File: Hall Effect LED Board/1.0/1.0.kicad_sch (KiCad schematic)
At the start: 5 parts, among them J1 Conn_01x04_Pin, U1 US5881LSE-AAA-000-RE

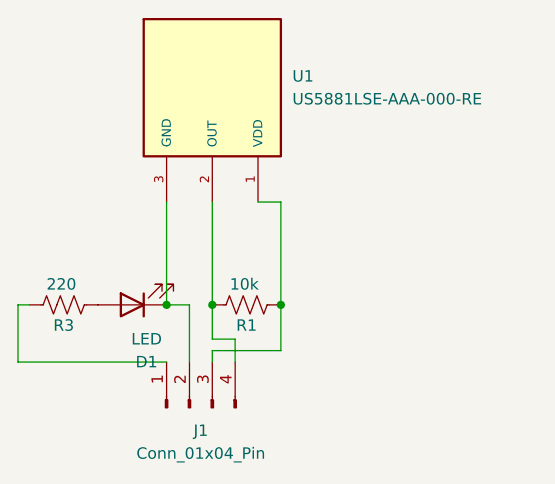
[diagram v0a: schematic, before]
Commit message: Set relative project specific components
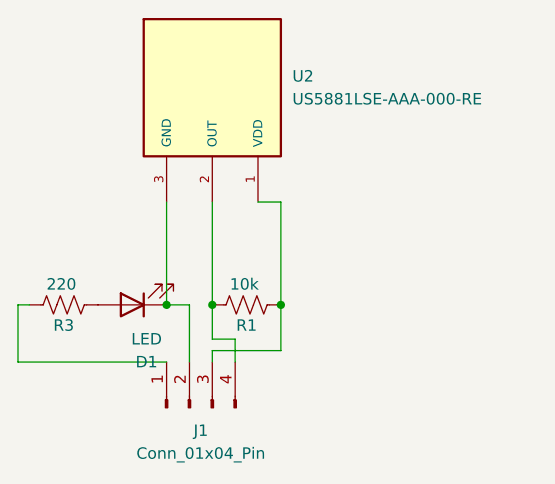
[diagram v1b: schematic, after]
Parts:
- removed U1: US5881LSE-AAA-000-RE, US5881LSE-AAA-000-RE:SOT95P280X100-3N, symbol US5881LSE-AAA-000-RE:US5881LSE-AAA-000-RE
- added U2: US5881LSE-AAA-000-RE, US5881LSE-AAA-000-RE:SOT95P280X100-3N, symbol US5881LSE-AAA-000-RE:US5881LSE-AAA-000-RE
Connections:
- net at J1.3 (Pin_3), R1.2: now also U2.1 (VDD)
- net at J1.4 (Pin_4), R1.1: now also U2.2 (OUT)
- net at D1.1 (K), J1.2 (Pin_2): now also U2.3 (GND)
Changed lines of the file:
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@@
-	)
-	(symbol
-		(lib_id "US5881LSE-AAA-000-RE:US5881LSE-AAA-000-RE")
-		(at 107.95 91.44 270)
-		(unit 1)
-		(exclude_from_sim no)
-		(in_bom yes)
-		(on_board yes)
-		(dnp no)
-		(fields_autoplaced yes)
-		(property "Reference" "U1"
-			(at 116.84 90.1699 90)
-			(effects
-				(font
-					(size 1.27 1.27)
-				)
-				(justify left)
-			)
-		)
-		(property "Value" "US5881LSE-AAA-000-RE"
-			(at 116.84 92.7099 90)
-			(effects
-				(font
-					(size 1.27 1.27)
-				)
-				(justify left)
-			)
-		)
-		(property "Footprint" "US5881LSE-AAA-000-RE:SOT95P280X100-3N"
-			(at 107.95 91.44 0)
-			(effects
-				(font
-					(size 1.27 1.27)
-				)
-				(justify bottom)
-				(hide yes)
-			)
-		)
-		(property "Datasheet" ""
-			(at 107.95 91.44 0)
-			(effects
-				(font
-					(size 1.27 1.27)
-				)
-				(hide yes)
-			)
-		)
-		(property "Description" ""
-			(at 107.95 91.44 0)
-			(effects
-				(font
-					(size 1.27 1.27)
-				)
-				(hide yes)
-			)
-		)
-		(property "MF" "Melexis"
-			(at 107.95 91.44 0)
-			(effects
-				(font
-					(size 1.27 1.27)
-				)
-				(justify bottom)
-				(hide yes)
-			)
-		)
-		(property "MAXIMUM_PACKAGE_HEIGHT" "1.00mm"
-			(at 107.95 91.44 0)
-			(effects
-				(font
-					(size 1.27 1.27)
-				)
-				(justify bottom)
-				(hide yes)
-			)
-		)
-		(property "Package" "TSOT-23L-3 Melexis"
-			(at 107.95 91.44 0)
-			(effects
-				(font
-					(size 1.27 1.27)
-				)
-				(justify bottom)
-				(hide yes)
-			)
-		)
-		(property "Price" "None"
-			(at 107.95 91.44 0)
-			(effects
-				(font
-					(size 1.27 1.27)
-				)
-				(justify bottom)
-				(hide yes)
-			)
-		)
-		(property "Check_prices" "https://www.snapeda.com/parts/US5881LSE-AAA-000-RE/Melexis/view-part/?ref=eda"
-			(at 107.95 91.44 0)
-			(effects
-				(font
-					(size 1.27 1.27)
-				)
-				(justify bottom)
-				(hide yes)
-			)
-		)
-		(property "STANDARD" "IPC-7351B"
-			(at 107.95 91.44 0)
-			(effects
-				(font
-					(size 1.27 1.27)
-				)
-				(justify bottom)
-				(hide yes)
-			)
-		)
-		(property "PARTREV" "005"
-			(at 107.95 91.44 0)
-			(effects
-				(font
-					(size 1.27 1.27)
-				)
-				(justify bottom)
-				(hide yes)
-			)
-		)
-		(property "SnapEDA_Link" "https://www.snapeda.com/parts/US5881LSE-AAA-000-RE/Melexis/view-part/?ref=snap"
-			(at 107.95 91.44 0)
-			(effects
-				(font
-					(size 1.27 1.27)
-				)
-				(justify bottom)
-				(hide yes)
-			)
-		)
-		(property "MP" "US5881LSE-AAA-000-RE"
-			(at 107.95 91.44 0)
-			(effects
-				(font
-					(size 1.27 1.27)
-				)
-				(justify bottom)
-				(hide yes)
-			)
-		)
-		(property "Description_1" "3 wire Latch"
-			(at 107.95 91.44 0)
-			(effects
-				(font
-					(size 1.27 1.27)
-				)
-				(justify bottom)
-				(hide yes)
-			)
-		)
-		(property "Availability" "In Stock"
-			(at 107.95 91.44 0)
-			(effects
-				(font
-					(size 1.27 1.27)
-				)
-				(justify bottom)
-				(hide yes)
-			)
-		)
-		(property "MANUFACTURER" "Melexis"
-			(at 107.95 91.44 0)
-			(effects
-				(font
-					(size 1.27 1.27)
-				)
-				(justify bottom)
-				(hide yes)
-			)
-		)
-		(pin "1"
-		)
-		(pin "3"
-		)
-		(pin "2"
-		)
-		(instances
-			(project ""
-				(path "/65e50814-7ec2-4aed-9027-cf46a8554e87"
-					(reference "U1")
-					(unit 1)
-				)
-			)
-		)
 	)
 	(symbol
@@
 					(unit 1)
 				)
+			)
+		)
+	)
+	(symbol
+		(lib_id "US5881LSE-AAA-000-RE:US5881LSE-AAA-000-RE")
+		(at 107.95 91.44 270)
+		(unit 1)
+		(exclude_from_sim no)
+		(in_bom yes)
+		(on_board yes)
+		(dnp no)
+		(fields_autoplaced yes)
+		(property "Reference" "U2"
+			(at 116.84 90.1699 90)
+			(effects
+				(font
+					(size 1.27 1.27)
+				)
+				(justify left)
+			)
+		)
+		(property "Value" "US5881LSE-AAA-000-RE"
+			(at 116.84 92.7099 90)
+			(effects
+				(font
+					(size 1.27 1.27)
+				)
+				(justify left)
+			)
+		)
+		(property "Footprint" "US5881LSE-AAA-000-RE:SOT95P280X100-3N"
+			(at 107.95 91.44 0)
+			(effects
+				(font
+					(size 1.27 1.27)
+				)
+				(justify bottom)
+				(hide yes)
+			)
+		)
+		(property "Datasheet" ""
+			(at 107.95 91.44 0)
+			(effects
+				(font
+					(size 1.27 1.27)
+				)
+				(hide yes)
+			)
+		)
+		(property "Description" ""
+			(at 107.95 91.44 0)
+			(effects
+				(font
+					(size 1.27 1.27)
+				)
+				(hide yes)
+			)
+		)
+		(property "MF" "Melexis"
+			(at 107.95 91.44 0)
+			(effects
+				(font
+					(size 1.27 1.27)
+				)
+				(justify bottom)
+				(hide yes)
+			)
+		)
+		(property "MAXIMUM_PACKAGE_HEIGHT" "1.00mm"
+			(at 107.95 91.44 0)
+			(effects
+				(font
+					(size 1.27 1.27)
+				)
+				(justify bottom)
+				(hide yes)
+			)
+		)
+		(property "Package" "TSOT-23L-3 Melexis"
+			(at 107.95 91.44 0)
+			(effects
+				(font
+					(size 1.27 1.27)
+				)
+				(justify bottom)
+				(hide yes)
+			)
+		)
+		(property "Price" "None"
+			(at 107.95 91.44 0)
+			(effects
+				(font
+					(size 1.27 1.27)
+				)
+				(justify bottom)
+				(hide yes)
+			)
+		)
+		(property "Check_prices" "https://www.snapeda.com/parts/US5881LSE-AAA-000-RE/Melexis/view-part/?ref=eda"
+			(at 107.95 91.44 0)
+			(effects
+				(font
+					(size 1.27 1.27)
+				)
+				(justify bottom)
+				(hide yes)
+			)
+		)
+		(property "STANDARD" "IPC-7351B"
+			(at 107.95 91.44 0)
+			(effects
+				(font
+					(size 1.27 1.27)
+				)
+				(justify bottom)
+				(hide yes)
+			)
+		)
+		(property "PARTREV" "005"
+			(at 107.95 91.44 0)
+			(effects
+				(font
+					(size 1.27 1.27)
+				)
+				(justify bottom)
+				(hide yes)
+			)
+		)
+		(property "SnapEDA_Link" "https://www.snapeda.com/parts/US5881LSE-AAA-000-RE/Melexis/view-part/?ref=snap"
+			(at 107.95 91.44 0)
+			(effects
+				(font
+					(size 1.27 1.27)
+				)
+				(justify bottom)
+				(hide yes)
+			)
+		)
+		(property "MP" "US5881LSE-AAA-000-RE"
+			(at 107.95 91.44 0)
+			(effects
+				(font
+					(size 1.27 1.27)
+				)
+				(justify bottom)
+				(hide yes)
+			)
+		)
+		(property "Description_1" "3 wire Latch"
+			(at 107.95 91.44 0)
+			(effects
+				(font
+					(size 1.27 1.27)
+				)
+				(justify bottom)
+				(hide yes)
+			)
+		)
+		(property "Availability" "In Stock"
+			(at 107.95 91.44 0)
+			(effects
+				(font
+					(size 1.27 1.27)
+				)
+				(justify bottom)
+				(hide yes)
+			)
+		)
+		(property "MANUFACTURER" "Melexis"
+			(at 107.95 91.44 0)
+			(effects
+				(font
+					(size 1.27 1.27)
+				)
+				(justify bottom)
+				(hide yes)
+			)
+		)
+		(pin "1"
+		)
+		(pin "3"
+		)
+		(pin "2"
+		)
+		(instances
+			(project ""
+				(path "/65e50814-7ec2-4aed-9027-cf46a8554e87"
+					(reference "U2")
+					(unit 1)
+				)
